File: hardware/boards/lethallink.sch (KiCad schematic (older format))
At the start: 11 parts, among them J1 PCIe-x4

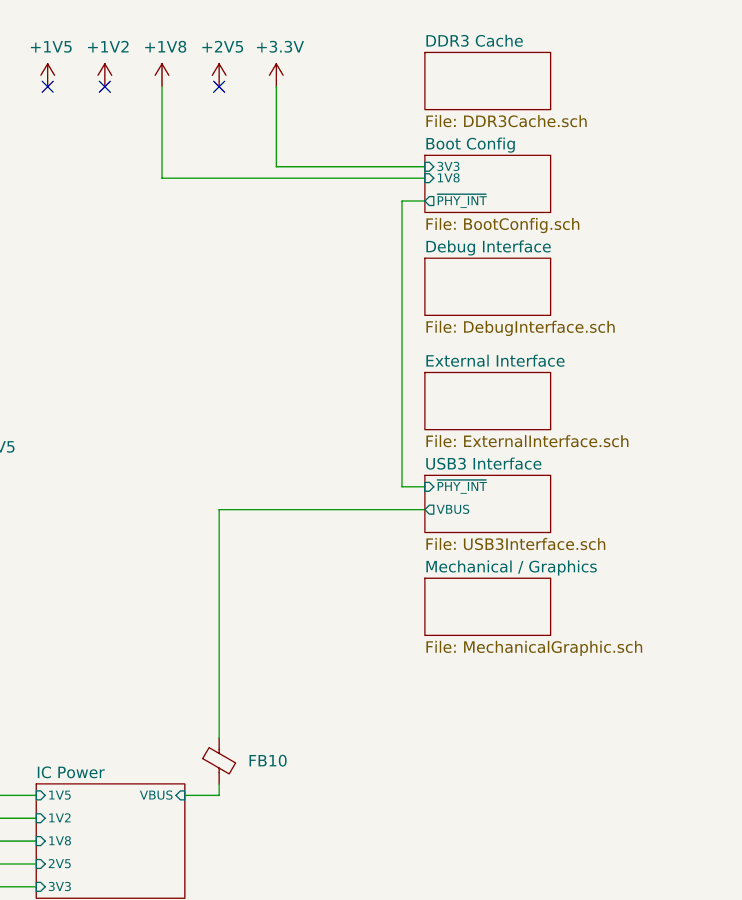
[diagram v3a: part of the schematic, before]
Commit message: Added headers for the SPI flash for both the FPGA and the PHY
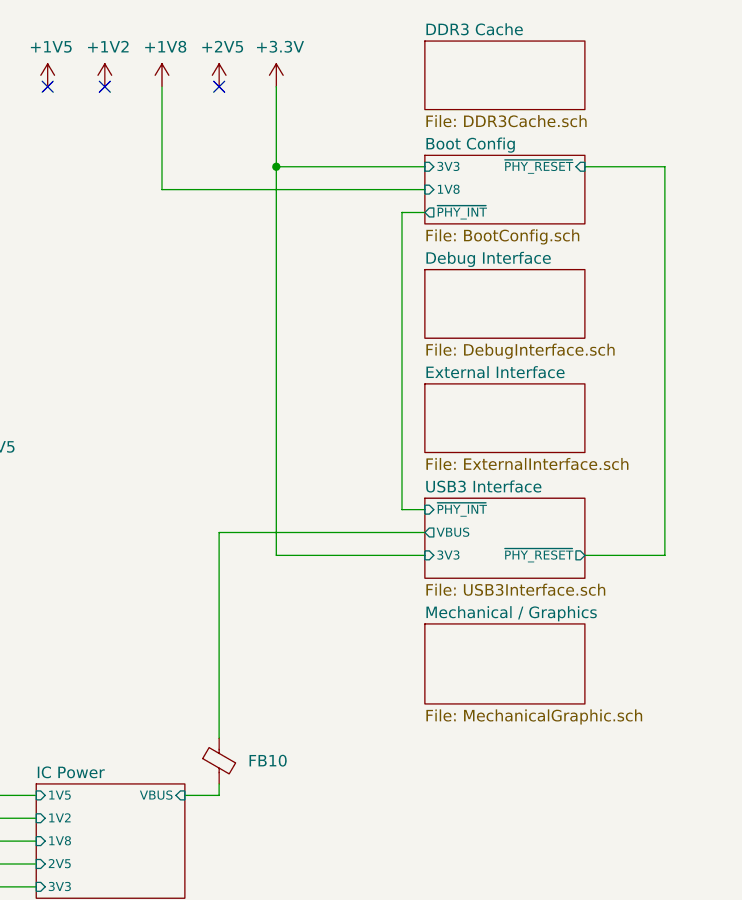
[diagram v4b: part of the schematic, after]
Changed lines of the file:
@@
 $EndDescr
 $Sheet
-S 14700 2050 550  250
+S 14700 2100 700  300
 U 5EF6A128
 F0 "External Interface" 50
@@
 $EndSheet
 $Sheet
-S 14700 1550 550  250
+S 14700 1600 700  300
 U 5EF67D90
 F0 "Debug Interface" 50
@@
 $EndSheet
 $Sheet
-S 14700 2950 550  250
+S 14700 3150 700  350
 U 5F55EF4C
 F0 "Mechanical / Graphics" 50
@@
 	8350 3900 9100 3900
 $Sheet
-S 14700 650  550  250
+S 14700 600  700  300
 U 5EDF3898
 F0 "DDR3 Cache" 50
@@
 $EndSheet
 $Sheet
-S 14700 1100 550  250
+S 14700 1100 700  300
 U 5EF66251
 F0 "Boot Config" 50
 F1 "BootConfig.sch" 50
 F2 "3V3" I L 14700 1150 39
-F3 "1V8" I L 14700 1200 39
-F4 "~PHY_INT" O L 14700 1300 39
+F3 "1V8" I L 14700 1250 39
+F4 "~PHY_INT" O L 14700 1350 39
+F5 "~PHY_RESET" I R 15400 1150 39
 $EndSheet
 Wire Wire Line
@@
 $EndComp
 Wire Wire Line
-	13550 1200 13550 800
-Wire Wire Line
-	13550 1200 14700 1200
+	13550 1250 13550 800
+Wire Wire Line
+	13550 1250 14700 1250
 NoConn ~ 13800 800
 NoConn ~ 13300 800
 NoConn ~ 13050 800
 Wire Wire Line
-	13800 3650 13800 2650
-Wire Wire Line
-	13800 2650 14700 2650
-$Sheet
-S 14700 2500 550  250
+	13800 3650 13800 2750
+Wire Wire Line
+	13800 2750 14700 2750
+$Sheet
+S 14700 2600 700  350
 U 5F2CAFD2
 F0 "USB3 Interface" 50
 F1 "USB3Interface.sch" 50
-F2 "VBUS" O L 14700 2650 39
-F3 "~PHY_INT" I L 14700 2550 39
-$EndSheet
-Wire Wire Line
-	14700 1300 14600 1300
-Wire Wire Line
-	14600 1300 14600 2550
-Wire Wire Line
-	14600 2550 14700 2550
+F2 "VBUS" O L 14700 2750 39
+F3 "~PHY_INT" I L 14700 2650 39
+F4 "~PHY_RESET" O R 15400 2850 39
+F5 "3V3" I L 14700 2850 39
+$EndSheet
+Wire Wire Line
+	14700 1350 14600 1350
+Wire Wire Line
+	14600 1350 14600 2650
+Wire Wire Line
+	14600 2650 14700 2650
+Wire Wire Line
+	15400 1150 15750 1150
+Wire Wire Line
+	15750 1150 15750 2850
+Wire Wire Line
+	15750 2850 15400 2850
+Wire Wire Line
+	14050 1150 14050 2850
+Wire Wire Line
+	14050 2850 14700 2850
+Connection ~ 14050 1150
 $EndSCHEMATC

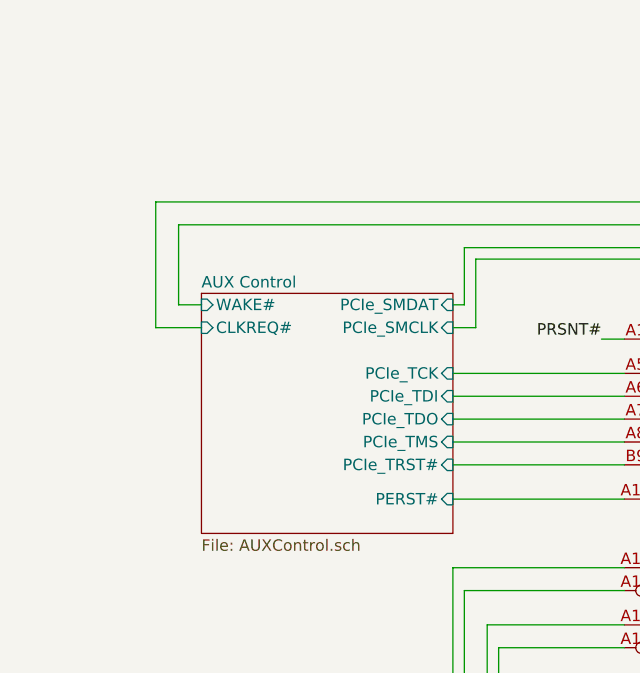
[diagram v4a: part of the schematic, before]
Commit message: Added the main OSC for the FPGA
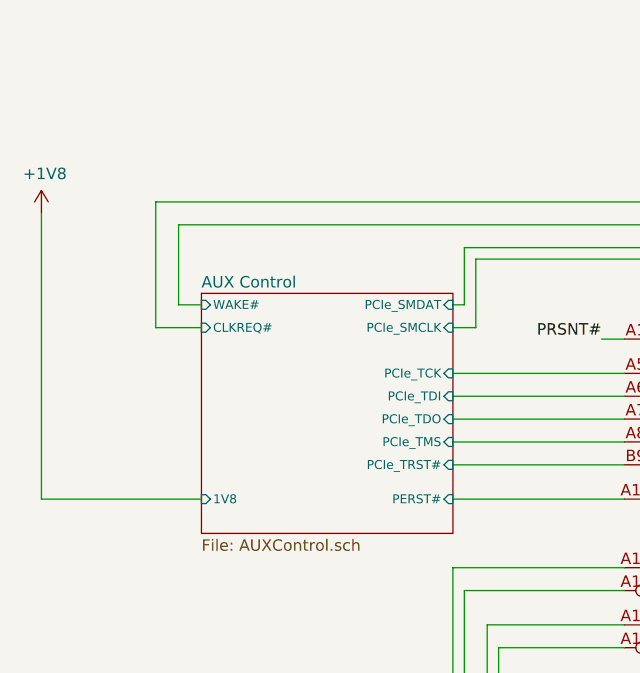
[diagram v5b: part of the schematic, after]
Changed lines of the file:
@@
 F0 "AUX Control" 50
 F1 "AUXControl.sch" 50
-F2 "PCIe_TCK" I R 6600 4050 50
-F3 "PCIe_TDI" I R 6600 4150 50
-F4 "PCIe_TDO" I R 6600 4250 50
-F5 "PCIe_TMS" I R 6600 4350 50
-F6 "PCIe_TRST#" I R 6600 4450 50
-F7 "PCIe_SMCLK" I R 6600 3850 50
-F8 "PCIe_SMDAT" I R 6600 3750 50
-F9 "PERST#" I R 6600 4600 50
-F10 "WAKE#" I L 5500 3750 50
-F11 "CLKREQ#" I L 5500 3850 50
+F2 "PCIe_TCK" I R 6600 4050 39
+F3 "PCIe_TDI" I R 6600 4150 39
+F4 "PCIe_TDO" I R 6600 4250 39
+F5 "PCIe_TMS" I R 6600 4350 39
+F6 "PCIe_TRST#" I R 6600 4450 39
+F7 "PCIe_SMCLK" I R 6600 3850 39
+F8 "PCIe_SMDAT" I R 6600 3750 39
+F9 "PERST#" I R 6600 4600 39
+F10 "WAKE#" I L 5500 3750 39
+F11 "CLKREQ#" I L 5500 3850 39
+F12 "1V8" I L 5500 4600 39
 $EndSheet
 Wire Wire Line
@@
 	14050 2850 14700 2850
 Connection ~ 14050 1150
+$Comp
+L power:+1V8 #PWR?
+U 1 1 611CD999
+P 4800 3350
+AR Path="/5EDF9F51/611CD999" Ref="#PWR?"  Part="1"
+AR Path="/611CD999" Ref="#PWR0139"  Part="1"
+F 0 "#PWR0139" H 4800 3200 50  0001 C CNN
+F 1 "+1V8" H 4815 3523 50  0000 C CNN
+F 2 "" H 4800 3350 50  0001 C CNN
+F 3 "" H 4800 3350 50  0001 C CNN
+	1    4800 3350
+	1    0    0    -1
+$EndComp
+Wire Wire Line
+	4800 4600 5500 4600
+Wire Wire Line
+	4800 3350 4800 4600
 $EndSCHEMATC

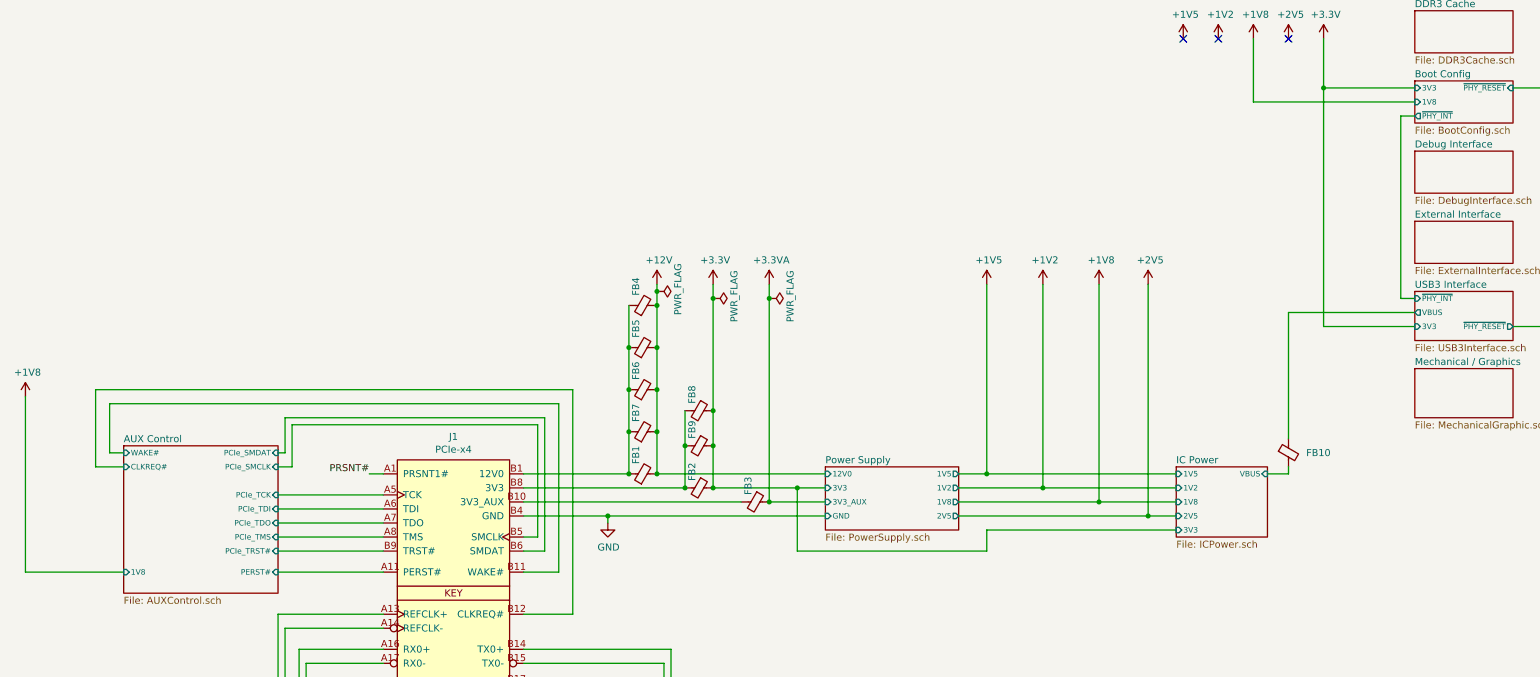
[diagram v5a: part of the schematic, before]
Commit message: Moved some more banks around to try and keeps things from crossing over as much as possible
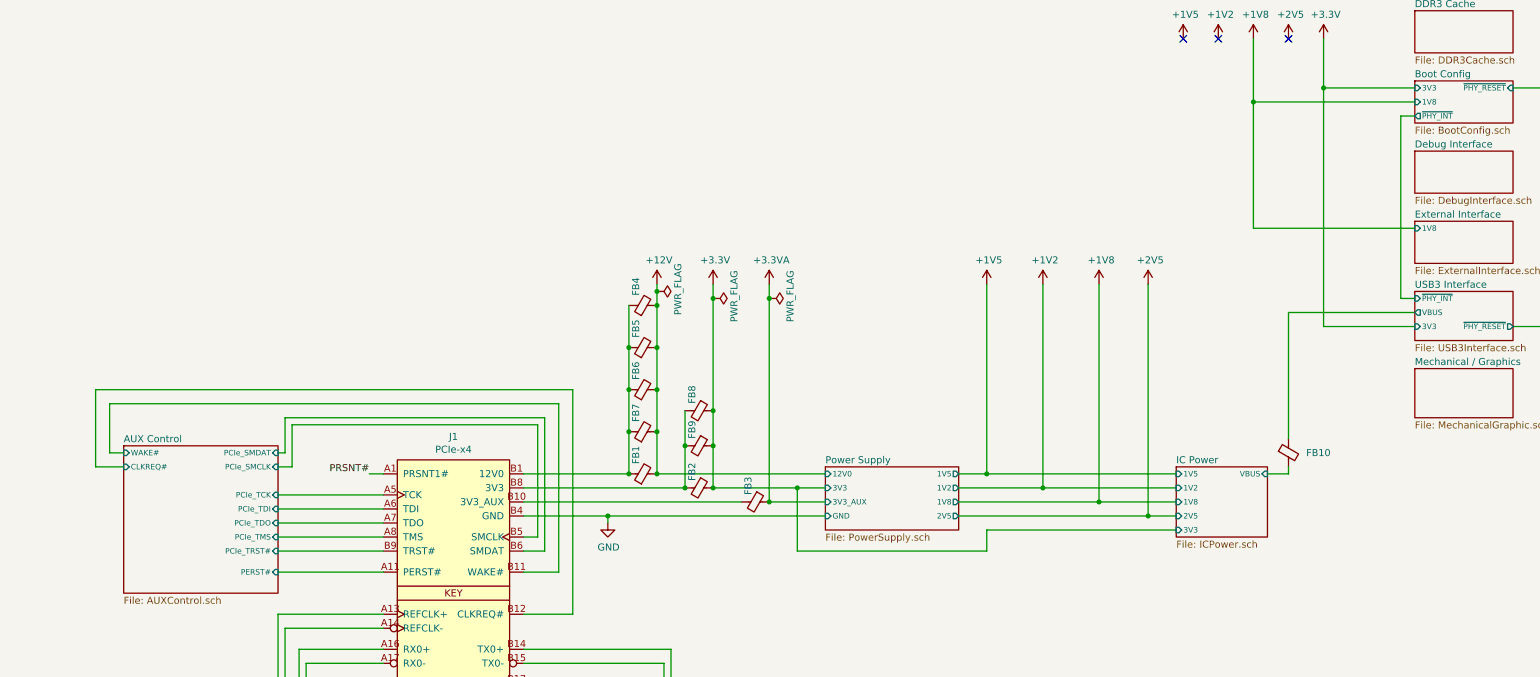
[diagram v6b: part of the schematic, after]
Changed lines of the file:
@@
 F0 "External Interface" 50
 F1 "ExternalInterface.sch" 50
+F2 "1V8" I L 14700 2150 39
 $EndSheet
 $Sheet
@@
 F10 "WAKE#" I L 5500 3750 39
 F11 "CLKREQ#" I L 5500 3850 39
-F12 "1V8" I L 5500 4600 39
 $EndSheet
 Wire Wire Line
@@
 	14050 2850 14700 2850
 Connection ~ 14050 1150
-$Comp
-L power:+1V8 #PWR?
-U 1 1 611CD999
-P 4800 3350
-AR Path="/5EDF9F51/611CD999" Ref="#PWR?"  Part="1"
-AR Path="/611CD999" Ref="#PWR0139"  Part="1"
-F 0 "#PWR0139" H 4800 3200 50  0001 C CNN
-F 1 "+1V8" H 4815 3523 50  0000 C CNN
-F 2 "" H 4800 3350 50  0001 C CNN
-F 3 "" H 4800 3350 50  0001 C CNN
-	1    4800 3350
-	1    0    0    -1
-$EndComp
-Wire Wire Line
-	4800 4600 5500 4600
-Wire Wire Line
-	4800 3350 4800 4600
+Wire Wire Line
+	13550 1250 13550 2150
+Wire Wire Line
+	13550 2150 14700 2150
+Connection ~ 13550 1250
 $EndSCHEMATC

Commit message: A batch of misc changes, I don't exactly recall what changed
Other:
- moved on the sheet: FB1, FB10, FB2, FB3, FB4, FB5, FB6, FB7, FB8, FB9, J1

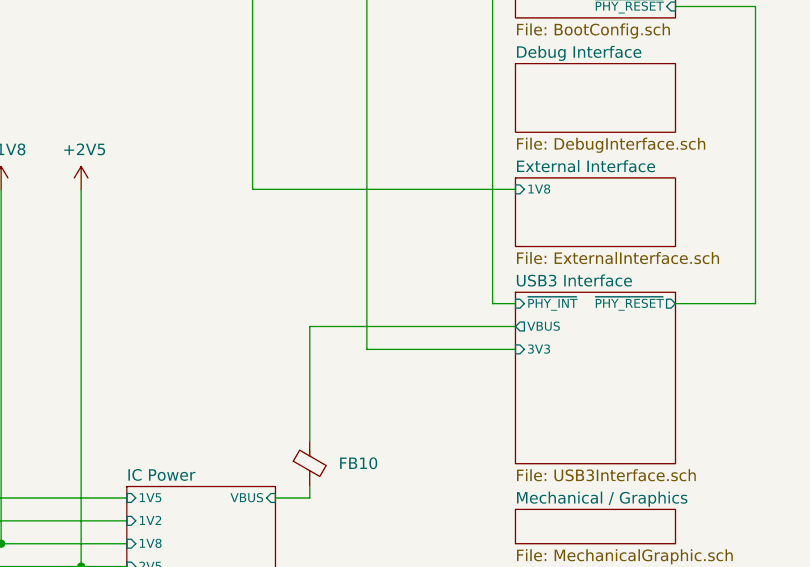
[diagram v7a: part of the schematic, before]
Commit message: Some messing about with the GPIF interface
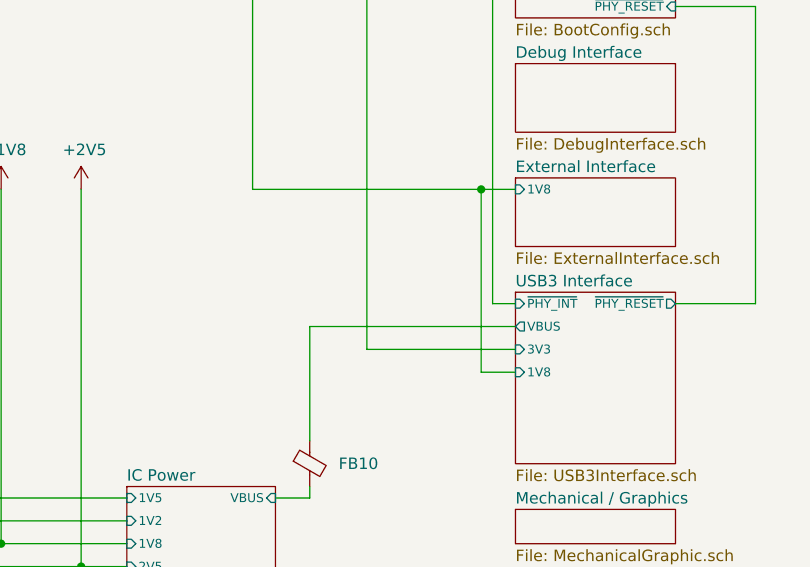
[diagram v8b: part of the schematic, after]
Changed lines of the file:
@@
 F4 "~PHY_RESET" O R 10750 3200 39
 F5 "3V3" I L 10050 3400 39
+F6 "1V8" I L 10050 3500 39
 $EndSheet
 Wire Wire Line
@@
 	8900 1350 8900 2700
 Wire Wire Line
-	8900 2700 10050 2700
+	8900 2700 9900 2700
 Connection ~ 8900 1350
+Wire Wire Line
+	9900 2700 9900 3500
+Wire Wire Line
+	9900 3500 10050 3500
+Connection ~ 9900 2700
+Wire Wire Line
+	9900 2700 10050 2700
 $EndSCHEMATC
